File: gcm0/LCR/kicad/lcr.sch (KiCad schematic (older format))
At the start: 84 parts, among them J1 Conn_01x02_Male, J2 Conn_01x02_Male, J3 Conn_01x03_Male, SW1 SW_Push, SW2 SW_Push, U1 MCP6022, U10 LM1117-3.3, U11 CD4052BCN, U2 HCF4053BE, U3 CD4052BCN, U4 LM317_TO-220, U5 MCP6022, U6 MCP6022, U7 LM358, U8 STM32F030F4P6, U9 74HC595, Y1 8MHZ

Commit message: SPI_74HC595
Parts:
- R22: value 1K -> 2K
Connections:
- net at DS1.4 (RS): now also U9.15 (QA); no longer U9.1 (QB)
- net at DS1.6 (E): now also U9.1 (QB); no longer U9.15 (QA)
- net PA7_SPI1_MOSI_74HC595_14_SER: now reaches R34.2, U9.14 (SER)
- net PA7_SPI1_MOSI_74HC595_14_SER: now also U8.13 (PA7); no longer U8.8 (PA2)
- net PA4_SPI1_NSS_74HC595_12_RCLK: now reaches R33.2, U9.12 (RCLK)
- net PA4_SPI1_NSS_74HC595_12_RCLK: now also U8.10 (PA4); no longer U8.7 (PA1)
- net PA5_SP1I_SCK_74HC595_11_SRCLK: now reaches R32.2, U9.11 (SRCLK)
- net PA5_SP1I_SCK_74HC595_11_SRCLK: now also U8.11 (PA5); no longer U8.6 (PA0)
- net PA0_ADC: now reaches C7.1, R23.1
- net PA0_ADC: now also U8.6 (PA0); no longer U8.10 (PA4)
- net PA5_4053_11 renamed PA1_4053_11
- net PA1_4053_11: now also U8.7 (PA1); no longer U8.11 (PA5)
- net PA6_4053_9_1I0 renamed PB1_4053_9_1I0
- net PB1_4053_9_1I0: now also U8.14 (PB1); no longer U8.12 (PA6)
- net PA7_4052_A renamed PA2_4052_A
- net PA2_4052_A: now also U8.8 (PA2); no longer U8.13 (PA7)
- net PB1_HC4052_B renamed PA6_HC4052_B
- net PA6_HC4052_B: now also U8.12 (PA6); no longer U8.14 (PB1)
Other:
- moved on the sheet: BT1, C1, C10, C11, C12, C13, C14, C15, C16, C17, C18, C19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

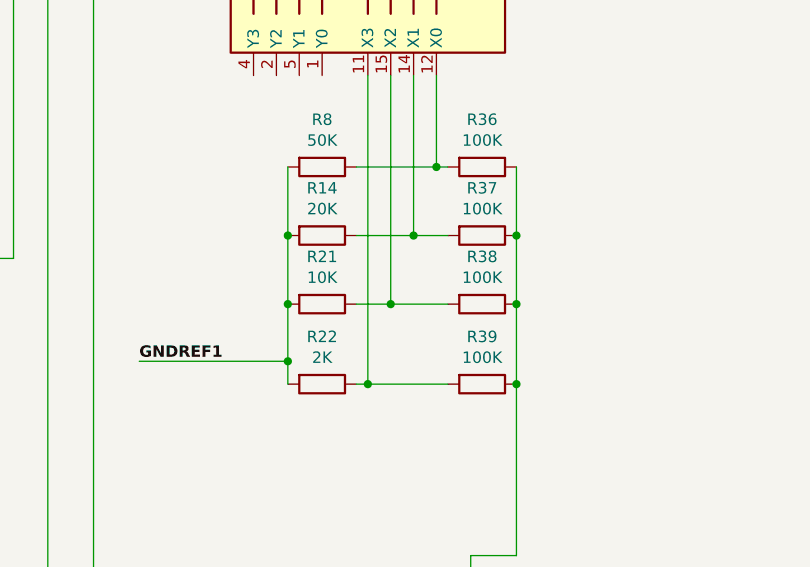
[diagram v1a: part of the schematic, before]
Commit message: 量程改错
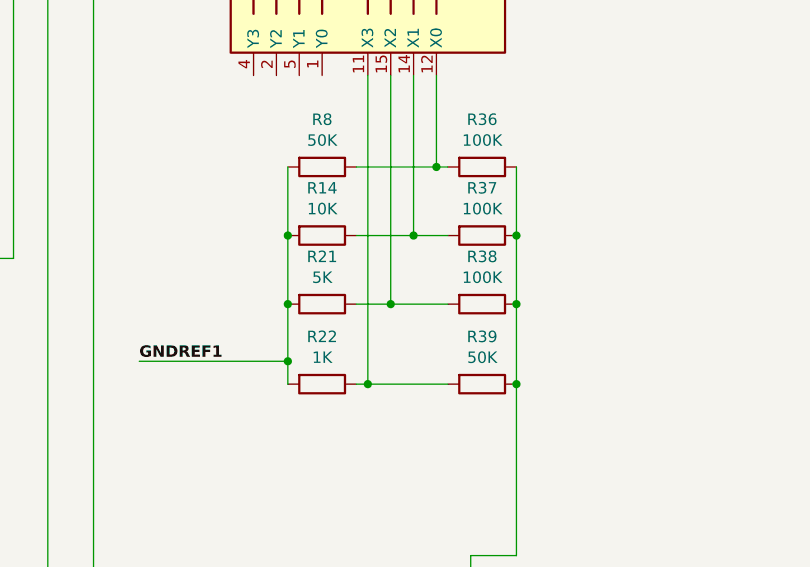
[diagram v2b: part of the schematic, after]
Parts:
- R14: value 20K -> 10K
- R21: value 10K -> 5K
- R22: value 2K -> 1K
- R39: value 100K -> 50K
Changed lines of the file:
@@
 P 9350 5650
 F 0 "R39" V 9143 5650 50  0000 C CNN
-F 1 "100K" V 9234 5650 50  0000 C CNN
+F 1 "50K" V 9234 5650 50  0000 C CNN
 F 2 "" V 9280 5650 50  0001 C CNN
 F 3 "~" H 9350 5650 50  0001 C CNN
@@
 P 8650 5000
 F 0 "R14" V 8443 5000 50  0000 C CNN
-F 1 "20K" V 8534 5000 50  0000 C CNN
+F 1 "10K" V 8534 5000 50  0000 C CNN
 F 2 "" V 8580 5000 50  0001 C CNN
 F 3 "~" H 8650 5000 50  0001 C CNN
@@
 P 8650 5300
 F 0 "R21" V 8443 5300 50  0000 C CNN
-F 1 "10K" V 8534 5300 50  0000 C CNN
+F 1 "5K" V 8534 5300 50  0000 C CNN
 F 2 "" V 8580 5300 50  0001 C CNN
 F 3 "~" H 8650 5300 50  0001 C CNN
@@
 P 8650 5650
 F 0 "R22" V 8443 5650 50  0000 C CNN
-F 1 "2K" V 8534 5650 50  0000 C CNN
+F 1 "1K" V 8534 5650 50  0000 C CNN
 F 2 "" V 8580 5650 50  0001 C CNN
 F 3 "~" H 8650 5650 50  0001 C CNN

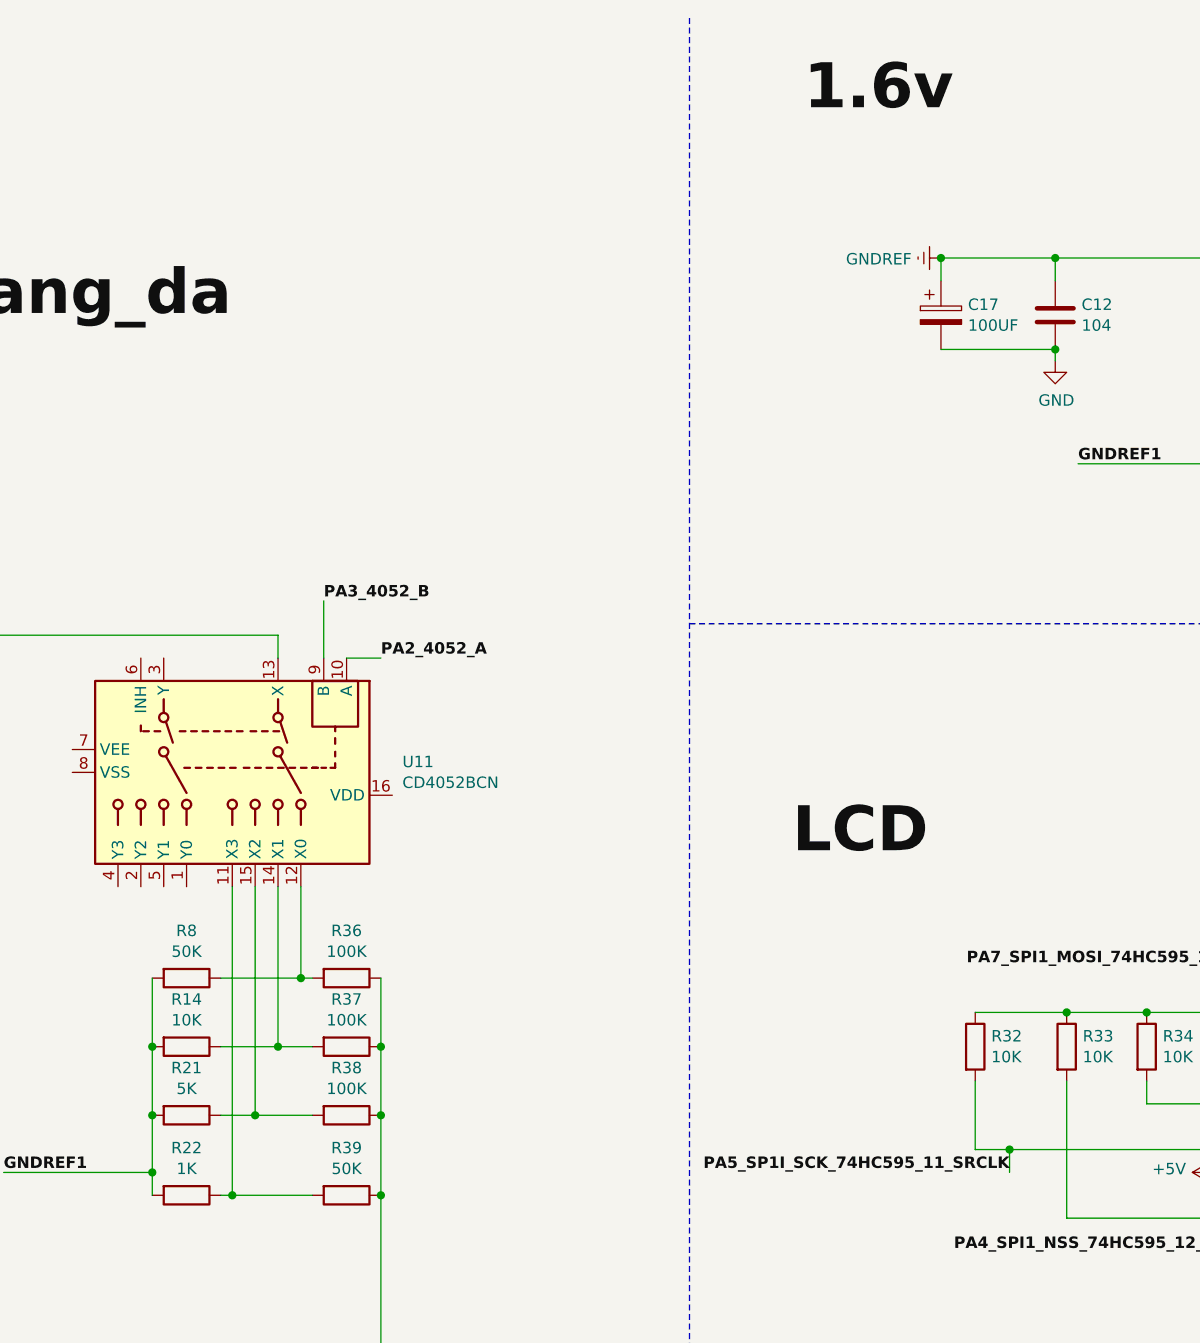
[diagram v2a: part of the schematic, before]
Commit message: 100KHZ自动量程
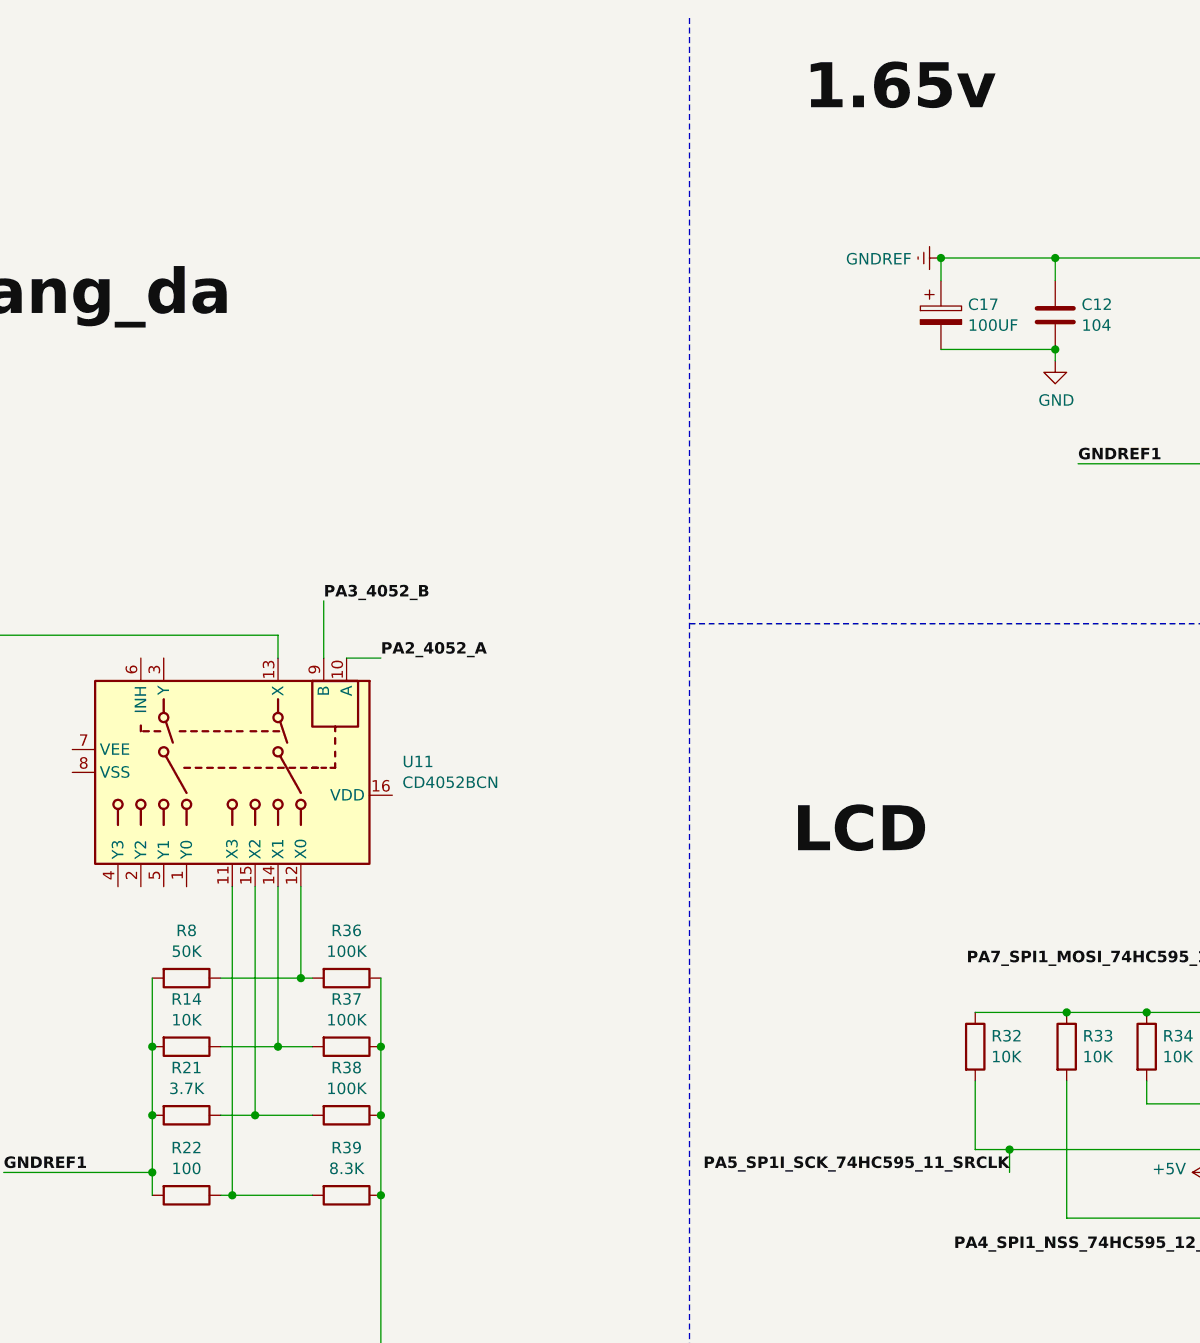
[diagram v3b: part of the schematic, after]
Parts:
- R21: value 5K -> 3.7K
- R22: value 1K -> 100
- R39: value 50K -> 8.3K
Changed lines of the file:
@@
 P 9350 5650
 F 0 "R39" V 9143 5650 50  0000 C CNN
-F 1 "50K" V 9234 5650 50  0000 C CNN
+F 1 "8.3K" V 9234 5650 50  0000 C CNN
 F 2 "" V 9280 5650 50  0001 C CNN
 F 3 "~" H 9350 5650 50  0001 C CNN
@@
 P 8650 5300
 F 0 "R21" V 8443 5300 50  0000 C CNN
-F 1 "5K" V 8534 5300 50  0000 C CNN
+F 1 "3.7K" V 8534 5300 50  0000 C CNN
 F 2 "" V 8580 5300 50  0001 C CNN
 F 3 "~" H 8650 5300 50  0001 C CNN
@@
 P 8650 5650
 F 0 "R22" V 8443 5650 50  0000 C CNN
-F 1 "1K" V 8534 5650 50  0000 C CNN
+F 1 "100" V 8534 5650 50  0000 C CNN
 F 2 "" V 8580 5650 50  0001 C CNN
 F 3 "~" H 8650 5650 50  0001 C CNN
@@
 	13150 8200 13350 8200
 Text Label 11350 950  0    197  ~ 39
-1.6v
+1.65v
 Text Label 11300 4200 0    197  ~ 39
 LCD

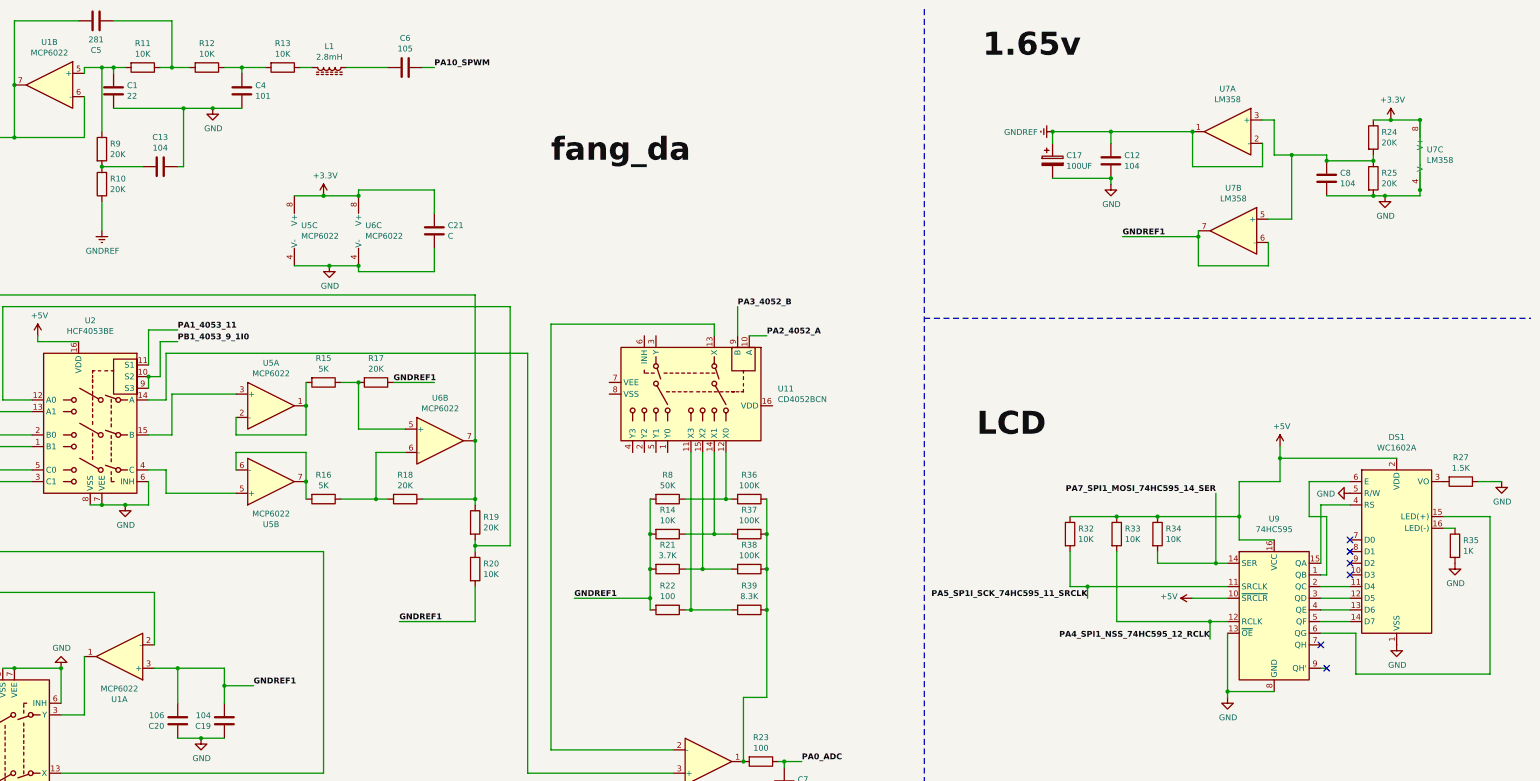
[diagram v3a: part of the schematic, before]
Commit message: 频率切换改错
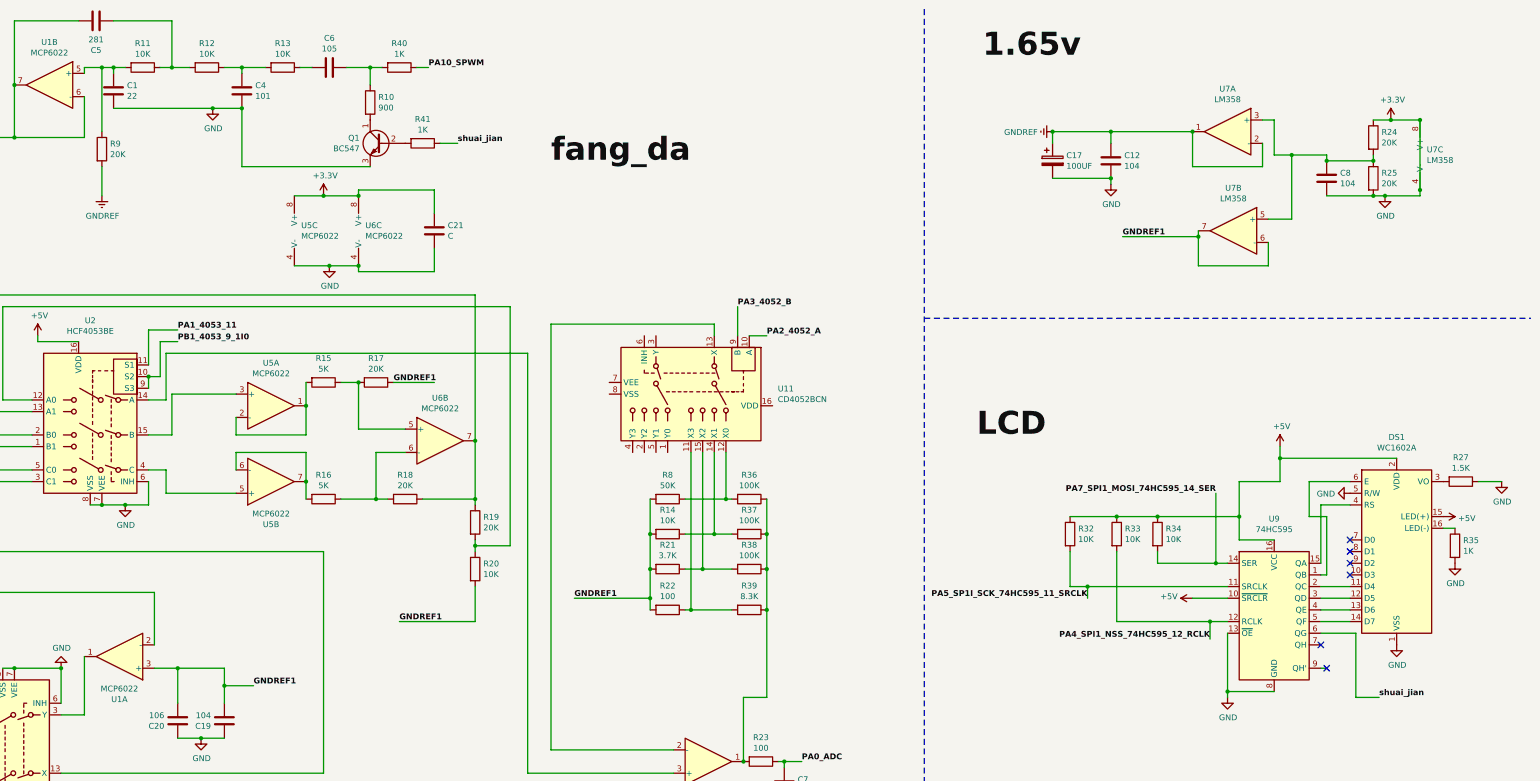
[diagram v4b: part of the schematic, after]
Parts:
- removed C13: 104, symbol Device:C
- removed L1: 2.8mH, symbol Device:L_Core_Ferrite
- added Q1: BC547, Package_TO_SOT_THT:TO-92_Inline, symbol Transistor_BJT:BC547
- added R40, R41: 1K, symbol Device:R
- R10: value 20K -> 900
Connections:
- net +3V3: now also Q1.3 (E)
- net +5V: now also DS1.15 (LED(+))
- net GNDREF: now also R9.2; no longer R10.1
- net PA10_SPWM: now also R40.1; no longer C6.1
- net at C6.2: now also R13.1
- net shuai_jian: now reaches U9.6 (QG)
- net shuai_jian: now also R41.1; no longer DS1.15 (LED(+))
- net at R10.2: now also Q1.1 (C); no longer R9.2
- new net: C6.1, R10.1, R40.2
- new net: Q1.2 (B), R41.2
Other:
- moved on the sheet: C6
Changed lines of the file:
@@
 L Device:C C6
 U 1 1 6103911D
-P 6400 1000
-F 0 "C6" V 6148 1000 50  0000 C CNN
-F 1 "105" V 6239 1000 50  0000 C CNN
-F 2 "" H 6438 850 50  0001 C CNN
-F 3 "~" H 6400 1000 50  0001 C CNN
-	1    6400 1000
+P 5750 1000
+F 0 "C6" V 5498 1000 50  0000 C CNN
+F 1 "105" V 5589 1000 50  0000 C CNN
+F 2 "" H 5788 850 50  0001 C CNN
+F 3 "~" H 5750 1000 50  0001 C CNN
+	1    5750 1000
 	0    1    1    0
 $EndComp
@@
 Wire Wire Line
 	13350 9100 13150 9100
-Text Label 6650 1000 0    50   ~ 10
+Text Label 6600 1000 0    50   ~ 10
 PA10_SPWM
 Text Label 13150 9000 2    50   ~ 10
@@
 L power:GNDREF #PWR019
 U 1 1 612A05B4
-P 3800 2400
-F 0 "#PWR019" H 3800 2150 50  0001 C CNN
-F 1 "GNDREF" H 3805 2227 50  0000 C CNN
-F 2 "" H 3800 2400 50  0001 C CNN
-F 3 "" H 3800 2400 50  0001 C CNN
-	1    3800 2400
+P 3800 2100
+F 0 "#PWR019" H 3800 1850 50  0001 C CNN
+F 1 "GNDREF" H 3805 1927 50  0000 C CNN
+F 2 "" H 3800 2100 50  0001 C CNN
+F 3 "" H 3800 2100 50  0001 C CNN
+	1    3800 2100
 	1    0    0    -1
 $EndComp
@@
 	3050 1600 3650 1600
 Connection ~ 3050 1600
-Wire Wire Line
-	3900 1350 4500 1350
 $Comp
 L Device:C C5
@@
 	4400 600  4400 1000
 Wire Wire Line
-	6650 1000 6550 1000
-$Comp
-L Device:L_Core_Ferrite L1
-U 1 1 612D4BA3
-P 5750 1000
-F 0 "L1" V 5569 1000 50  0000 C CNN
-F 1 "2.8mH" V 5660 1000 50  0000 C CNN
-F 2 "" H 5750 1000 50  0001 C CNN
-F 3 "~" H 5750 1000 50  0001 C CNN
-	1    5750 1000
-	0    1    1    0
-$EndComp
+	6600 1000 6500 1000
 Wire Wire Line
 	5600 1000 5500 1000
@@
 	1    0    0    -1
 $EndComp
-$Comp
-L Device:R R10
-U 1 1 61300FC2
-P 3800 2000
-F 0 "R10" H 3730 1954 50  0000 R CNN
-F 1 "20K" H 3730 2045 50  0000 R CNN
-F 2 "" V 3730 2000 50  0001 C CNN
-F 3 "~" H 3800 2000 50  0001 C CNN
-	1    3800 2000
-	-1   0    0    1
-$EndComp
-$Comp
-L Device:C C13
-U 1 1 61379779
-P 4300 1850
-F 0 "C13" V 4048 1850 50  0000 C CNN
-F 1 "104" V 4139 1850 50  0000 C CNN
-F 2 "" H 4338 1700 50  0001 C CNN
-F 3 "~" H 4300 1850 50  0001 C CNN
-	1    4300 1850
-	0    1    1    0
-$EndComp
-Wire Wire Line
-	4150 1850 3800 1850
-Wire Wire Line
-	4450 1850 4500 1850
-Wire Wire Line
-	4500 1850 4500 1350
-Connection ~ 4500 1350
-Wire Wire Line
-	4500 1350 4750 1350
 Wire Wire Line
 	3800 1550 3800 1000
@@
 Wire Wire Line
 	5450 10000 6000 10000
-Connection ~ 3800 1850
-Wire Wire Line
-	3800 2150 3800 2400
+Wire Wire Line
+	3800 1850 3800 2100
 Wire Wire Line
 	3050 600  3050 1150
@@
 Wire Wire Line
 	15300 4950 15400 4950
-Wire Wire Line
-	15700 4850 15300 4850
 NoConn ~ 14250 5950
 Wire Wire Line
@@
 Wire Wire Line
 	1800 4550 1800 5500
-Wire Wire Line
-	14550 5850 14550 6200
-Wire Wire Line
-	14550 6200 15700 6200
-Wire Wire Line
-	15700 6200 15700 4850
 Wire Wire Line
 	14250 5850 14550 5850
@@
 Text Label 7650 1850 0    197  ~ 39
 fang_da
-Wire Wire Line
-	5900 1000 6250 1000
 Text Label 13150 8200 2    50   ~ 10
 PA0_ADC
@@
 Wire Wire Line
 	14150 4550 14500 4550
+Wire Wire Line
+	3900 1350 4750 1350
+$Comp
+L Device:R R40
+U 1 1 612F6685
+P 6350 1000
+F 0 "R40" V 6143 1000 50  0000 C CNN
+F 1 "1K" V 6234 1000 50  0000 C CNN
+F 2 "" V 6280 1000 50  0001 C CNN
+F 3 "~" H 6350 1000 50  0001 C CNN
+	1    6350 1000
+	0    1    1    0
+$EndComp
+$Comp
+L Device:R R10
+U 1 1 612F8045
+P 6100 1300
+F 0 "R10" H 6170 1346 50  0000 L CNN
+F 1 "900" H 6170 1255 50  0000 L CNN
+F 2 "" V 6030 1300 50  0001 C CNN
+F 3 "~" H 6100 1300 50  0001 C CNN
+	1    6100 1300
+	1    0    0    -1
+$EndComp
+Wire Wire Line
+	6100 1150 6100 1000
+Wire Wire Line
+	5900 1000 6100 1000
+Connection ~ 6100 1000
+Wire Wire Line
+	6100 1000 6200 1000
+$Comp
+L Transistor_BJT:BC547 Q1
+U 1 1 61365E54
+P 6200 1650
+F 0 "Q1" H 6391 1696 50  0000 L CNN
+F 1 "BC547" H 6391 1605 50  0000 L CNN
+F 2 "Package_TO_SOT_THT:TO-92_Inline" H 6400 1575 50  0001 L CIN
+F 3 "https://www.onsemi.com/pub/Collateral/BC550-D.pdf" H 6200 1650 50  0001 L CNN
+	1    6200 1650
+	-1   0    0    -1
+$EndComp
+Wire Wire Line
+	6100 1850 5000 1850
+Wire Wire Line
+	5000 1850 5000 1350
+Connection ~ 5000 1350
+$Comp
+L Device:R R41
+U 1 1 613D792F
+P 6550 1650
+F 0 "R41" V 6343 1650 50  0000 C CNN
+F 1 "1K" V 6434 1650 50  0000 C CNN
+F 2 "" V 6480 1650 50  0001 C CNN
+F 3 "~" H 6550 1650 50  0001 C CNN
+	1    6550 1650
+	0    1    1    0
+$EndComp
+Wire Wire Line
+	6700 1650 6850 1650
+Text Label 6850 1650 0    50   ~ 10
+shuai_jian
+Text Label 14750 6400 0    50   ~ 10
+shuai_jian
+Wire Wire Line
+	14550 6400 14750 6400
+Wire Wire Line
+	14550 5850 14550 6400
+$Comp
+L power:+5V #PWR08
+U 1 1 61507F5E
+P 15300 4850
+F 0 "#PWR08" H 15300 4700 50  0001 C CNN
+F 1 "+5V" V 15315 4978 50  0000 L CNN
+F 2 "" H 15300 4850 50  0001 C CNN
+F 3 "" H 15300 4850 50  0001 C CNN
+	1    15300 4850
+	0    1    1    0
+$EndComp
 $EndSCHEMATC

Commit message: 频率切换改错1
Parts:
- added C13: 104, symbol Device:C
- added Q2: BC547, Package_TO_SOT_THT:TO-92_Inline, symbol Transistor_BJT:BC547
- added R42, R43: 1K, symbol Device:R
- C1: value 22 -> 104
- C4: value 101 -> 102
- C5: value 281 -> 102
- C6: value 105 -> 102
- R10: value 900 -> 200
- R11, R12, R13: value 10K -> 1K
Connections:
- net +3V3: now also C5.2, C6.2, Q2.3 (E); no longer C1.2
- net at C1.1, R9.1, U1.5 (+): no longer R11.2
- net at R6.1, U1.6 (-), U1.7: no longer C5.2
- net at R10.1, R40.2: now also R43.1; no longer C6.1
- net at R13.1: now also C13.1, R43.2; no longer C6.2
- net at R12.1, R13.2: now also C6.1; no longer C4.1
- net shuai_jian1: now reaches U9.7 (QH)
- net shuai_jian1: now also R42.2
- new net: C13.2, Q2.1 (C)
- new net: Q2.2 (B), R42.1
- new net: C1.2, C4.1, R11.2
- no-connect marks 6 -> 5
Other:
- moved on the sheet: C21, Q1, R10, R40, R41, U5C, U6C
